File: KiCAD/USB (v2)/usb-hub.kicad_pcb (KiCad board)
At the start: 2 copper layers, 22.4 x 24.2 mm, 22 parts, among them J1 046809610110846+ Male, J3 Conn_01x04_Socket, U1 CY7C65634-28LTXC, Y1 12MHz 18pF

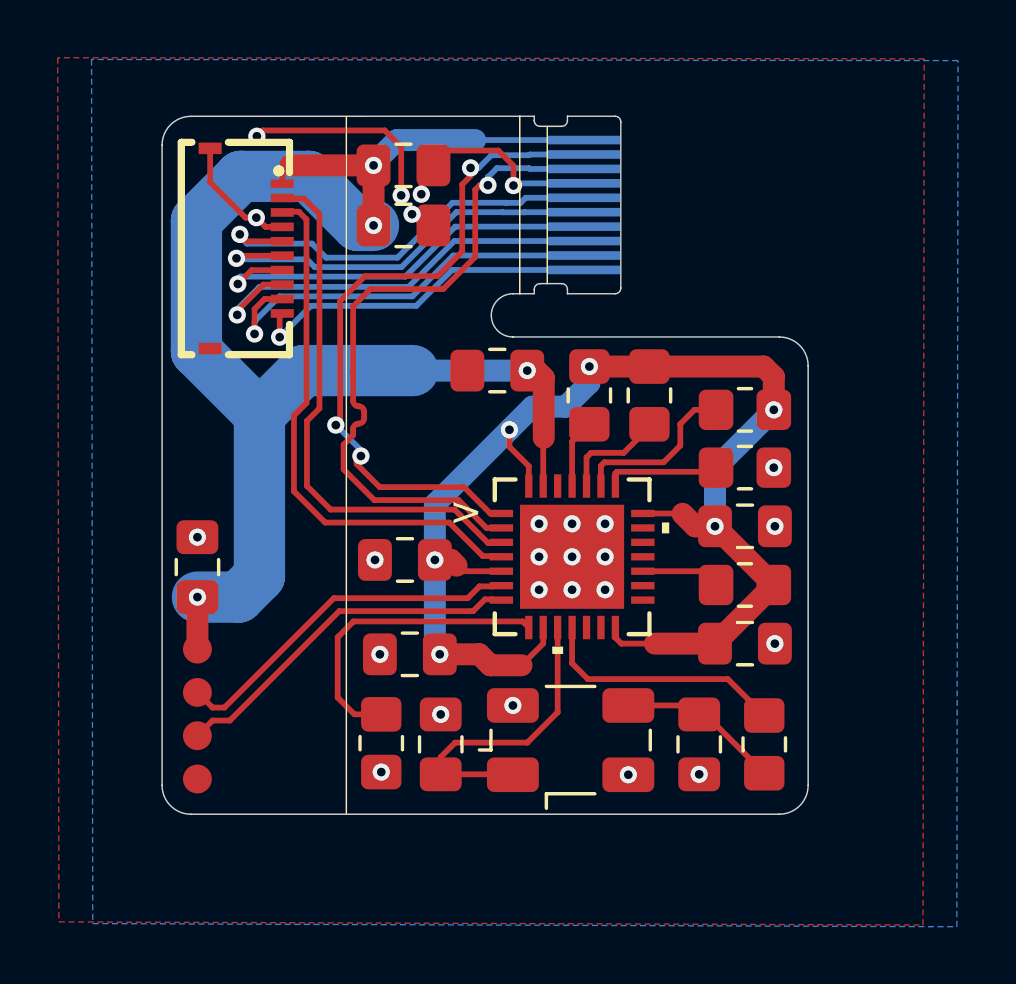
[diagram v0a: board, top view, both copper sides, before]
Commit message: bigger pads
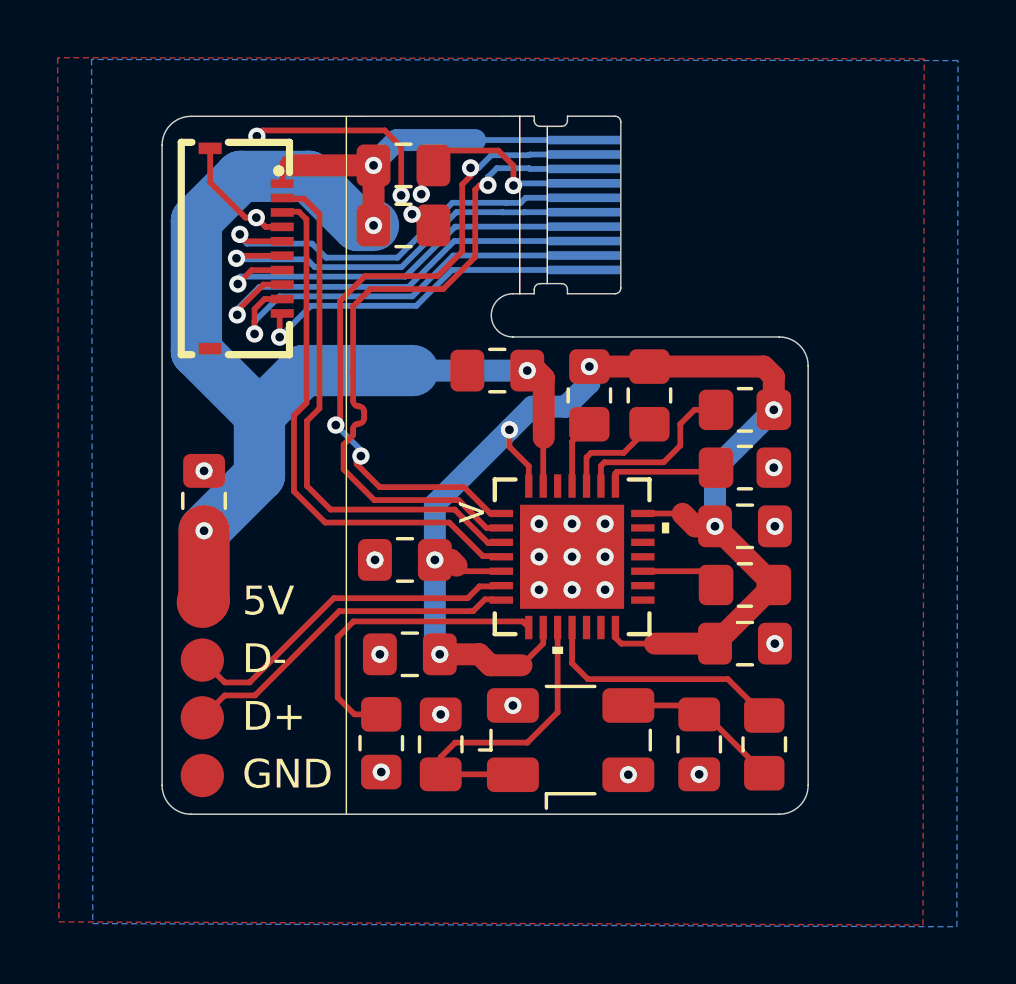
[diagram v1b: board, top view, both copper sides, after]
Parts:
- moved C8 2.31 mm to (135.1, 45.3)
- moved J3 0.89 mm to (135.0, 51.8)
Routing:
- net VBUS: track 52.7 -> 50.2 mm
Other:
- board text added: "5V"
- board text added: "D+"
- board text added: "D-"
- board text added: "GND"
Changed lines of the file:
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@@
 	(footprint "Custom:4 pad"
 		(layer "F.Cu")
-		(at 134.85 52.71 -90)
+		(at 135.02 51.84 -90)
 		(property "Reference" "J3"
 			(at 0 -1.75 270)
@@
 		)
 		(pad "1" smd circle
-			(at -2.25 0 270)
-			(size 1 1)
+			(at -3 0 270)
+			(size 1.5 1.5)
 			(layers "F.Cu" "F.Mask" "F.Paste")
 			(net 4 "VBUS")
@@
 		)
 		(pad "2" smd circle
-			(at -0.75 0 270)
-			(size 1 1)
+			(at -1 0 270)
+			(size 1.5 1.5)
 			(layers "F.Cu" "F.Mask" "F.Paste")
 			(net 16 "USB_KB_N")
@@
 		)
 		(pad "3" smd circle
-			(at 0.75 0 270)
-			(size 1 1)
+			(at 1 0 270)
+			(size 1.5 1.5)
 			(layers "F.Cu" "F.Mask" "F.Paste")
 			(net 15 "USB_KB_P")
@@
 		)
 		(pad "4" smd circle
-			(at 2.25 0 270)
-			(size 1 1)
+			(at 3 0 270)
+			(size 1.5 1.5)
 			(layers "F.Cu" "F.Mask" "F.Paste")
 			(net 9 "GND")
@@
 	(footprint "Capacitor_SMD:C_0805_2012Metric_Pad1.18x1.45mm_HandSolder"
 		(layer "F.Cu")
-		(at 134.85 47.62 -90)
+		(at 135.08 45.3225 -90)
 		(descr "Capacitor SMD 0805 (2012 Metric), square (rectangular) end terminal, IPC-7351 nominal with elongated pad for handsoldering. (Body size source: IPC-SM-782 page 76, https://www.pcb-3d.com/wordpress/wp-content/uploads/ipc-sm-782a_amendment_1_and_2.pdf, https://docs.google.com/spreadsheets/d/1BsfQQcO9C6DZCsRaXUlFlo91Tg2WpOkGARC1WS5S8t0/edit?usp=sharing), generated with kicad-footprint-generator")
 		(tags "capacitor handsolder")
@@
 		)
 		(fp_text user ">"
-			(at -3.6811 -1.5611 0)
+			(at -3.4811 -1.5711 0)
 			(unlocked yes)
 			(layer "F.SilkS")
@@
 			)
 		)
-		(fp_text user "*"
-			(at -2.0447 -1.75 0)
+		(fp_text user "${REFERENCE}"
+			(at 0 0 0)
 			(unlocked yes)
 			(layer "F.Fab")
@@
 			)
 		)
-		(fp_text user "${REFERENCE}"
-			(at 0 0 0)
+		(fp_text user "*"
+			(at -2.0447 -1.75 0)
 			(unlocked yes)
 			(layer "F.Fab")
@@
 		)
 		(group ""
-			(members "10ff2fe7-edf6-4f5e-9fb1-4be25c92da2a" "1a08e7d1-cd63-44c0-abd6-dca92062c1e0"
-				"291f6b8d-77a7-415b-834b-dc27f2473a30" "311aaf29-9333-4770-ba09-a40b89955e5c"
-				"361ec015-1c89-4c1e-a3a3-f1b6670d3214" "36374e34-8981-4b7c-a368-153cdb50482a"
-				"38a1fbe0-f524-4a80-86c7-44519e7ce32a" "56e7a9ad-fe4d-4ed7-87a8-a08ccaae7351"
-				"7660c143-a043-4efc-8b44-0168e9efd00b" "8a2bb285-a807-4191-93ed-9267a3062203"
-				"9806acb4-f2ab-4ca9-b3a6-32cc056fb12b" "9e218311-484e-44c8-8871-9f6a372ee941"
-				"c3f2c8b1-5eef-446c-8b9f-e0391f29394d" "c59e5fab-e285-46d6-8aa4-150457586ba0"
-				"d02a75a5-1e0f-47f5-95c3-52ead3db2b9e" "d523de1f-81c5-48ad-b132-aa4736ae8fea"
-				"da63f7cf-e549-4c11-9f1c-6034d14e8de9" "e541f8aa-1938-48ae-ab87-5bd069cdda6f"
-				"f6f80154-c634-4ba2-9674-bfa4cfe648db" "fc6ded9d-3527-446e-82d9-9f1a6448a7cc"
+			(members "07960ab5-e2d9-4597-a9ba-f0c3aaf9eee7" "174daff6-a1db-43fa-ae3c-fc45ec941db0"
+				"21580439-599e-4d00-be87-d8d26e6aeb0f" "28c24501-4f9b-4e3e-9b37-36d4e2a66e3b"
+				"2df0d187-7512-4f18-a961-b655f92fe3d8" "3acaebf0-e176-43fd-920f-2c16f7cdd857"
+				"44cee516-6267-446c-b107-c414108a1a6d" "51ae2238-9f7a-4229-adfe-30de87a4ad85"
+				"53ad3e62-9bd7-49c2-ac57-8a11e22d1484" "56d25903-521e-42da-b0e8-809096c942d9"
+				"5c43ea4e-f5a9-41d1-a611-701e1e0bbe49" "83ae6359-3369-4dec-addf-776bfc67ddab"
+				"8a30e783-57a0-4389-ae12-c623c5860d40" "91409e90-e2f4-4dde-8b74-066f08f6f4b0"
+				"a2f3221a-8f63-4eed-9bda-f2aec0d966aa" "c7999fc3-31b1-49cd-993b-633b311fa050"
+				"d752f623-6bb4-4b79-8cfd-41517c3b3c04" "db839d2e-afa9-4d80-8bca-654e6fd97e17"
+				"ddb6e0a0-274b-4379-b522-0764b8799bc3" "e815023d-820a-42d0-a6ef-2ebd44e99300"
 			)
 		)
@@
 		(layer "User.1")
 	)
+	(gr_text "D+"
+		(at 136.4 53.3795 0)
+		(layer "F.SilkS")
+		(effects
+			(font
+				(size 1 1)
+				(thickness 0.1)
+			)
+			(justify left bottom)
+		)
+	)
+	(gr_text "5V"
+		(at 136.4 49.3795 0)
+		(layer "F.SilkS")
+		(effects
+			(font
+				(size 1 1)
+				(thickness 0.1)
+			)
+			(justify left bottom)
+		)
+	)
+	(gr_text "GND"
+		(at 136.4 55.3795 0)
+		(layer "F.SilkS")
+		(effects
+			(font
+				(size 1 1)
+				(thickness 0.1)
+			)
+			(justify left bottom)
+		)
+	)
+	(gr_text "D-"
+		(at 136.4 51.3795 0)
+		(layer "F.SilkS")
+		(effects
+			(font
+				(size 1 1)
+				(thickness 0.1)
+			)
+			(justify left bottom)
+		)
+	)
 	(gr_text "JLCJLCJLCJLC"
 		(at 133.84 50.21 270)
@@
 	)
 	(segment
+		(start 135.08 46.36)
+		(end 135.08 48.78)
+		(width 1.778)
+		(layer "F.Cu")
+		(net 4)
+	)
+	(segment
 		(start 140.9525 33.7)
 		(end 138.07 33.7)
@@
 	)
 	(segment
-		(start 134.85 50.46)
-		(end 134.85 48.6575)
-		(width 0.762)
-		(layer "F.Cu")
-		(net 4)
-	)
-	(segment
 		(start 137.79 34.33)
 		(end 137.79 33.98)
@@
 		(net 4)
 	)
+	(segment
+		(start 135.08 48.78)
+		(end 135.02 48.84)
+		(width 1.778)
+		(layer "F.Cu")
+		(net 4)
+	)
 	(via
 		(at 140.9525 35.78)
@@
 	)
 	(via
-		(at 134.85 48.6575)
+		(at 135.08 46.36)
 		(size 0.6)
 		(drill 0.3)
@@
 	)
 	(segment
-		(start 134.85 48.6575)
-		(end 136.2725 48.6575)
-		(width 1.778)
-		(layer "B.Cu")
-		(net 4)
-	)
-	(segment
 		(start 137 42.33)
 		(end 138.52 40.81)
@@
 	)
 	(segment
-		(start 136.2725 48.6575)
-		(end 137 47.93)
-		(width 1.778)
-		(layer "B.Cu")
-		(net 4)
-	)
-	(segment
 		(start 140.9525 33.6375)
 		(end 141.7675 32.8225)
@@
 	)
 	(segment
-		(start 137 47.93)
-		(end 137 42.33)
+		(start 137 42.33)
+		(end 137 44.44)
 		(width 1.778)
 		(layer "B.Cu")
@@
 	)
 	(segment
+		(start 137 44.44)
+		(end 135.08 46.36)
+		(width 1.778)
+		(layer "B.Cu")
+		(net 4)
+	)
+	(segment
 		(start 140.41 35.78)
 		(end 138.71 34.08)
@@
 	)
 	(via
-		(at 141.1725 50.64)
+		(at 135.08 44.285)
 		(size 0.6)
 		(drill 0.3)
@@
 	)
 	(via
-		(at 147.8311 48.4041)
+		(at 141.1725 50.64)
 		(size 0.6)
 		(drill 0.3)
@@
 	)
 	(via
-		(at 146.6881 46.1181)
+		(at 147.8311 48.4041)
 		(size 0.6)
 		(drill 0.3)
@@
 	)
 	(via
-		(at 134.85 46.5825)
+		(at 146.6881 46.1181)
 		(size 0.6)
 		(drill 0.3)
@@
 	)
 	(segment
-		(start 135.973197 52.935001)
-		(end 135.374999 52.935001)
+		(start 139.763198 49.145)
+		(end 136.843197 52.065001)
 		(width 0.2)
 		(layer "F.Cu")
@@
 	)
 	(segment
-		(start 139.763198 49.145)
-		(end 135.973197 52.935001)
-		(width 0.2)
-		(layer "F.Cu")
-		(net 15)
-	)
-	(segment
-		(start 135.374999 52.935001)
-		(end 134.85 53.46)
+		(start 136.843197 52.065001)
+		(end 135.794999 52.065001)
 		(width 0.2)
 		(layer "F.Cu")
@@
 	)
 	(segment
-		(start 135.786803 52.484999)
-		(end 135.374999 52.484999)
+		(start 135.794999 52.065001)
+		(end 135.02 52.84)
 		(width 0.2)
 		(layer "F.Cu")
-		(net 16)
+		(net 15)
 	)
 	(segment
@@
 	)
 	(segment
-		(start 135.374999 52.484999)
-		(end 134.85 51.96)
+		(start 136.656803 51.614999)
+		(end 135.794999 51.614999)
 		(width 0.2)
 		(layer "F.Cu")
@@
 	(segment
 		(start 139.576802 48.695)
-		(end 135.786803 52.484999)
+		(end 136.656803 51.614999)
+		(width 0.2)
+		(layer "F.Cu")
+		(net 16)
+	)
+	(segment
+		(start 135.794999 51.614999)
+		(end 135.02 50.84)
 		(width 0.2)
 		(layer "F.Cu")

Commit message: what
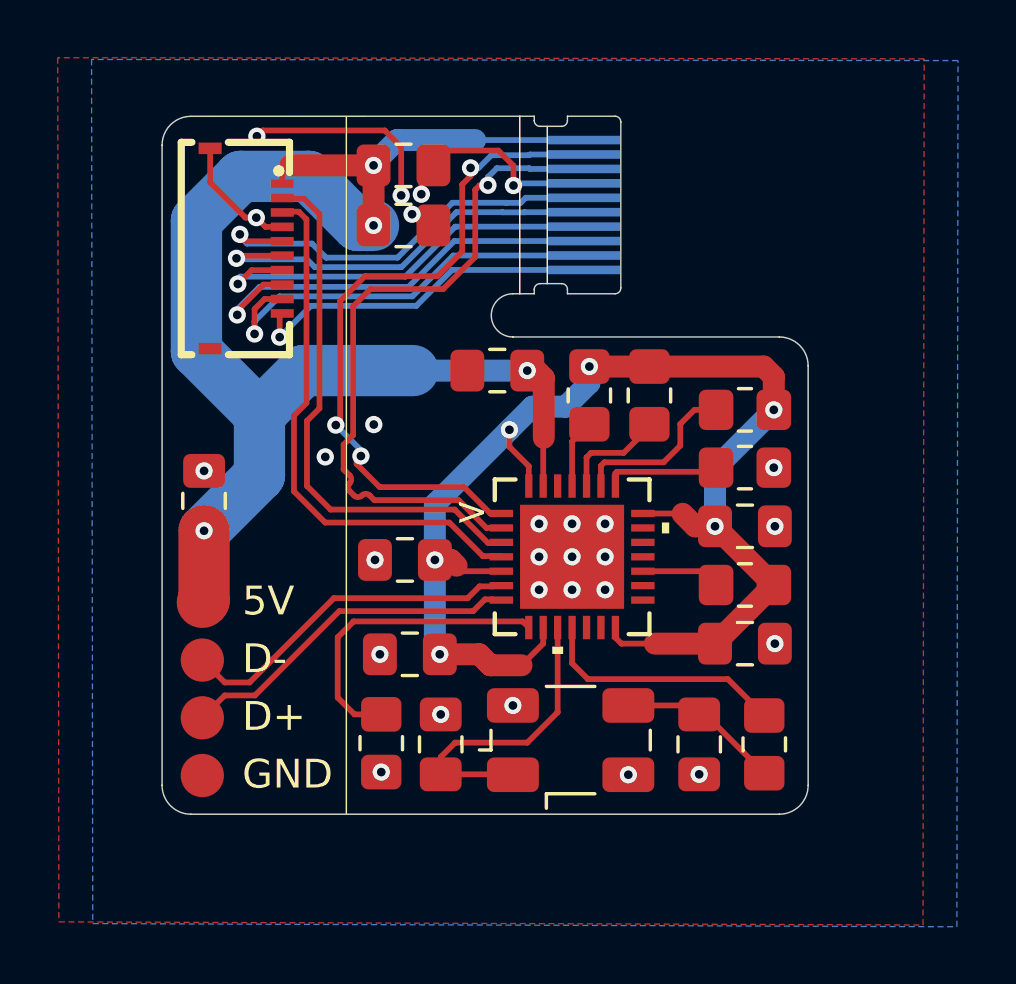
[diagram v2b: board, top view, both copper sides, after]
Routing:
- net GND: vias 26 -> 28
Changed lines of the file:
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@@
 	)
 	(segment
-		(start 140.628052 42.455652)
-		(end 140.628052 42.238704)
+		(start 144.863159 46.261099)
+		(end 143.89906 45.297)
+		(width 0.2)
+		(layer "F.Cu")
+		(net 5)
+	)
+	(segment
+		(start 139.915 44.233198)
+		(end 139.915 44.220676)
+		(width 0.2)
+		(layer "F.Cu")
+		(net 5)
+	)
+	(segment
+		(start 140.245 38.583198)
+		(end 140.843198 37.985)
+		(width 0.2)
+		(layer "F.Cu")
+		(net 5)
+	)
+	(segment
+		(start 144.475 36.873198)
+		(end 144.475 34.545743)
+		(width 0.2)
+		(layer "F.Cu")
+		(net 5)
+	)
+	(segment
+		(start 139.915 43.375)
+		(end 140.245 43.045)
+		(width 0.2)
+		(layer "F.Cu")
+		(net 5)
+	)
+	(segment
+		(start 144.475 34.545743)
+		(end 144.632488 34.388255)
+		(width 0.2)
+		(layer "F.Cu")
+		(net 5)
+	)
+	(segment
+		(start 140.277239 45.137125)
+		(end 140.123818 44.983704)
 		(width 0.2)
 		(layer "F.Cu")
@@
 	)
 	(segment
-		(start 144.475 34.545743)
-		(end 144.632488 34.388255)
-		(width 0.2)
-		(layer "F.Cu")
-		(net 5)
-	)
-	(segment
-		(start 144.863159 46.261099)
-		(end 143.89906 45.297)
-		(width 0.2)
-		(layer "F.Cu")
-		(net 5)
-	)
-	(segment
-		(start 140.978802 45.297)
-		(end 139.915 44.233198)
+		(start 143.363198 37.985)
+		(end 144.475 36.873198)
+		(width 0.2)
+		(layer "F.Cu")
+		(net 5)
+	)
+	(segment
+		(start 140.245 43.045)
+		(end 140.245 38.583198)
 		(width 0.2)
 		(layer "F.Cu")
@@
 	)
 	(segment
-		(start 140.245 41.855652)
-		(end 140.245 41.638704)
-		(width 0.2)
-		(layer "F.Cu")
-		(net 5)
-	)
-	(segment
-		(start 140.245 43.045)
-		(end 140.245 42.838704)
-		(width 0.2)
-		(layer "F.Cu")
-		(net 5)
-	)
-	(segment
-		(start 139.915 44.233198)
+		(start 139.970398 44.288596)
+		(end 139.915 44.233198)
+		(width 0.2)
+		(layer "F.Cu")
+		(net 5)
+	)
+	(segment
+		(start 140.123818 44.442016)
+		(end 139.970398 44.288596)
+		(width 0.2)
+		(layer "F.Cu")
+		(net 5)
+	)
+	(segment
+		(start 143.89906 45.297)
+		(end 140.978802 45.297)
+		(width 0.2)
+		(layer "F.Cu")
+		(net 5)
+	)
+	(segment
+		(start 140.978802 45.297)
+		(end 140.818927 45.137125)
+		(width 0.2)
+		(layer "F.Cu")
+		(net 5)
+	)
+	(segment
+		(start 139.915 44.220676)
 		(end 139.915 43.375)
-		(width 0.2)
-		(layer "F.Cu")
-		(net 5)
-	)
-	(segment
-		(start 144.475 36.873198)
-		(end 144.475 34.545743)
-		(width 0.2)
-		(layer "F.Cu")
-		(net 5)
-	)
-	(segment
-		(start 140.245 41.638704)
-		(end 140.245 40.895294)
-		(width 0.2)
-		(layer "F.Cu")
-		(net 5)
-	)
-	(segment
-		(start 139.915 43.375)
-		(end 140.245 43.045)
 		(width 0.2)
 		(layer "F.Cu")
@@
 		(net 5)
 	)
-	(segment
-		(start 140.245 38.583198)
-		(end 140.843198 37.985)
-		(width 0.2)
-		(layer "F.Cu")
-		(net 5)
-	)
-	(segment
-		(start 143.89906 45.297)
-		(end 140.978802 45.297)
-		(width 0.2)
-		(layer "F.Cu")
-		(net 5)
-	)
-	(segment
-		(start 140.245 40.895294)
-		(end 140.245 38.583198)
-		(width 0.2)
-		(layer "F.Cu")
-		(net 5)
-	)
-	(segment
-		(start 143.363198 37.985)
-		(end 144.475 36.873198)
-		(width 0.2)
-		(layer "F.Cu")
-		(net 5)
-	)
 	(via
 		(at 144.915331 34.388255)
@@
 	)
 	(arc
-		(start 140.436526 42.647178)
-		(mid 140.571955 42.591081)
-		(end 140.628052 42.455652)
+		(start 140.818927 45.137125)
+		(mid 140.683505 45.081031)
+		(end 140.548083 45.137125)
 		(width 0.2)
 		(layer "F.Cu")
@@
 	)
 	(arc
-		(start 140.628052 42.238704)
-		(mid 140.571955 42.103275)
-		(end 140.436526 42.047178)
+		(start 140.123818 44.71286)
+		(mid 140.179912 44.577438)
+		(end 140.123818 44.442016)
 		(width 0.2)
 		(layer "F.Cu")
@@
 	)
 	(arc
-		(start 140.436526 42.047178)
-		(mid 140.301097 41.991081)
-		(end 140.245 41.855652)
+		(start 140.548083 45.137125)
+		(mid 140.412661 45.193219)
+		(end 140.277239 45.137125)
 		(width 0.2)
 		(layer "F.Cu")
@@
 	)
 	(arc
-		(start 140.245 42.838704)
-		(mid 140.301097 42.703275)
-		(end 140.436526 42.647178)
+		(start 140.123818 44.983704)
+		(mid 140.067724 44.848282)
+		(end 140.123818 44.71286)
 		(width 0.2)
 		(layer "F.Cu")
@@
 		(drill 0.3)
 		(layers "F.Cu" "B.Cu")
+		(net 9)
+	)
+	(via
+		(at 140.96 42.68)
+		(size 0.6)
+		(drill 0.3)
+		(layers "F.Cu" "B.Cu")
+		(free yes)
+		(net 9)
+	)
+	(via
+		(at 139.28 43.8)
+		(size 0.6)
+		(drill 0.3)
+		(layers "F.Cu" "B.Cu")
+		(free yes)
 		(net 9)
 	)
@@
 		(base_line
 			(pts
-				(xy 140.245 42.838704) (xy 140.245 40.895294)
+				(xy 140.818927 45.137125) (xy 139.915 44.233198) (xy 139.915 44.220676)
 			)
 		)
 		(base_line_coupled
 			(pts
-				(xy 140.118584 43.171416) (xy 140.245 43.045) (xy 140.245 42.547831)
+				(xy 141.137125 44.818927) (xy 141.124191 44.805993)
 			)
 		)
 		(corner_radius_percent 80)
 		(end
-			(xy 140.245 40.895294)
+			(xy 139.915 44.220676)
 		)
-		(initial_side "right")
+		(initial_side "left")
 		(last_diff_pair_gap 0.18)
 		(last_netname "USB_HOST_P")
@@
 		(min_spacing 0.6)
 		(origin
-			(xy 140.245 42.838704)
+			(xy 140.818927 45.137125)
 		)
 		(override_custom_rules no)
@@
 		(target_skew_min -0.1)
 		(tuning_mode "diff_pair_skew")
-		(members "0601fb30-e24e-4d15-bea7-361788267380" "6cb1d7d9-e363-4942-bbf4-6ec9d0ae32dd"
-			"76a2b182-0f1c-4b6f-a474-ada6e05beb60" "7a3eb374-6210-4264-9512-3cc9f40bfde7"
-			"805b1cdd-d2db-43e1-90d8-af874953d323" "936be9d1-586d-4b18-856b-c9b3ed0b1db6"
-			"d484da3e-0759-41ec-925b-205289cdba1d"
+		(members "08e7138d-493a-473a-8c27-e0279e0cfce5" "384ca064-2e32-4176-b3d6-07bb774c9e9a"
+			"54e348df-338d-4632-b411-2626e376c459" "678f7a32-142e-4352-90a8-70d4355b69f3"
+			"6b78ce0b-e989-40ed-9b39-86d19f1790b7" "82862134-14ea-4384-b1d2-3c787815cebe"
+			"b7f3b18c-9620-4b0c-94dc-2eff1fc2d7ec" "b9031e3c-eb11-437a-8518-f0cd434fe516"
 		)
 	)
